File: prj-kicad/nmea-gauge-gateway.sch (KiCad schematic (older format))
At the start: 2 parts, among them P1 CONN_M12-5, P2 CONN_8

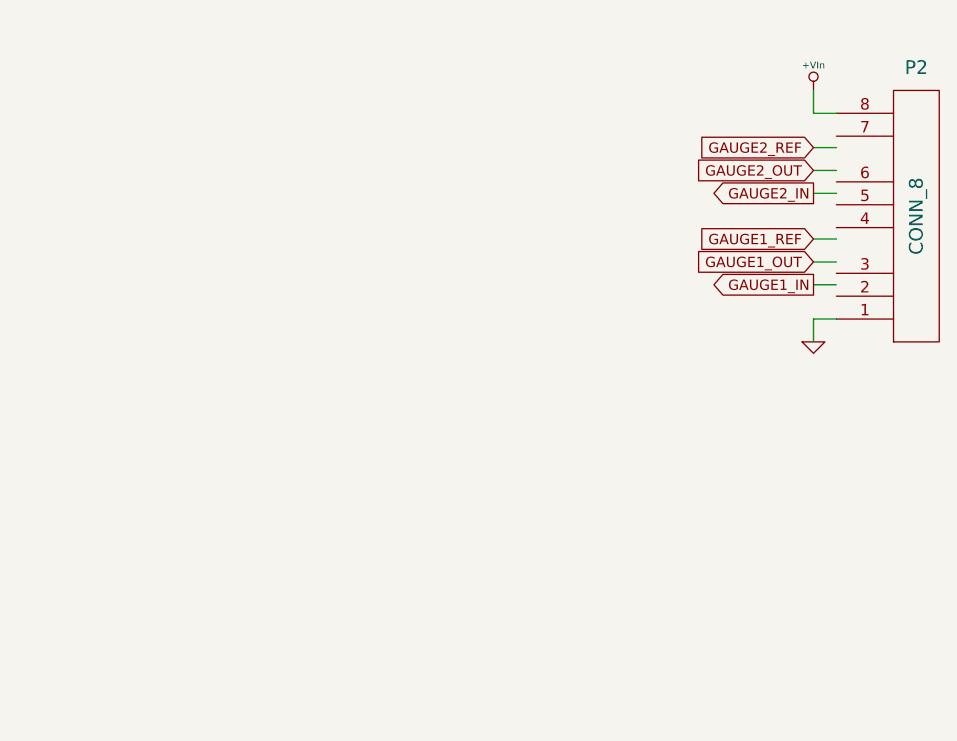
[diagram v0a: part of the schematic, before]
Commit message: = ADD: Insert analog inputs/outputs for gauge sensors
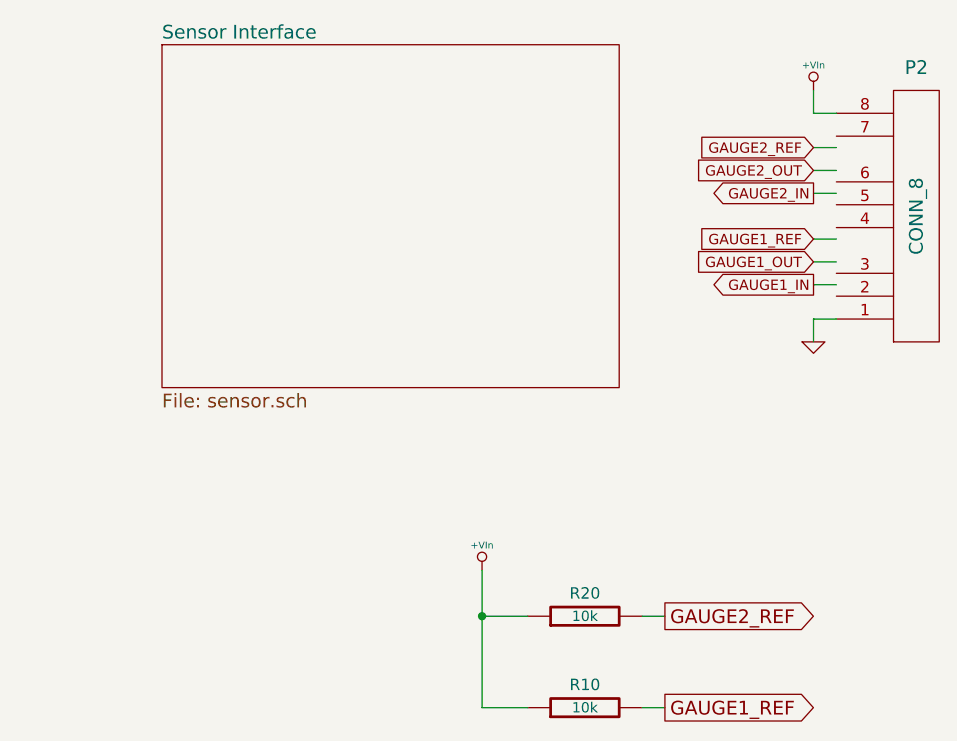
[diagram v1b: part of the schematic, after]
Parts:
- added R10, R20: 10k, nmea-gauge-gateway:SMD0805, symbol R
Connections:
- wire segments 10 -> 15
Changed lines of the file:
@@
 $Descr A4 11693 8268
 encoding utf-8
-Sheet 1 1
+Sheet 1 2
 Title "NMEA2000 Gauge Gateway"
 Date "2020-04-04"
@@
 F 0 "P1" H 1400 3700 60  0000 C CNN
 F 1 "CONN_M12-5" H 1400 3000 45  0000 C CNN
-F 2 "" H 1400 3350 60  0000 C CNN
+F 2 "" H 1400 3350 60  0001 C CNN
 F 3 "" H 1400 3350 60  0000 C CNN
 	1    1400 3350
 	-1   0    0    -1
 $EndComp
+$Comp
+L R R20
+U 1 1 5E9B72F1
+P 8600 5100
+F 0 "R20" V 8700 5100 50  0000 C CNN
+F 1 "10k" V 8600 5100 45  0000 C CNN
+F 2 "nmea-gauge-gateway:SMD0805" H 8600 5100 60  0001 C CNN
+F 3 "" H 8600 5100 60  0000 C CNN
+	1    8600 5100
+	0    -1   -1   0
+$EndComp
+$Comp
+L R R10
+U 1 1 5E9B7320
+P 8600 5500
+F 0 "R10" V 8700 5500 50  0000 C CNN
+F 1 "10k" V 8600 5500 45  0000 C CNN
+F 2 "nmea-gauge-gateway:SMD0805" H 8600 5500 60  0001 C CNN
+F 3 "" H 8600 5500 60  0000 C CNN
+	1    8600 5500
+	0    -1   -1   0
+$EndComp
+$Comp
+L +VIn #PWR03
+U 1 1 5E9B73E0
+P 8150 4900
+F 0 "#PWR03" H 8150 4860 30  0001 C CNN
+F 1 "+VIn" H 8150 5010 30  0000 C CNN
+F 2 "" H 8150 4900 60  0000 C CNN
+F 3 "" H 8150 4900 60  0000 C CNN
+	1    8150 4900
+	1    0    0    -1
+$EndComp
+Text GLabel 8950 5500 2    60   Output ~ 0
+GAUGE1_REF
+Wire Wire Line
+	8950 5500 8850 5500
+Wire Wire Line
+	8950 5100 8850 5100
+Text GLabel 8950 5100 2    60   Output ~ 0
+GAUGE2_REF
+Wire Wire Line
+	8150 4900 8150 5500
+Wire Wire Line
+	8150 5500 8350 5500
+Wire Wire Line
+	8350 5100 8150 5100
+Connection ~ 8150 5100
+$Sheet
+S 6750 2600 2000 1500
+U 5E920088
+F0 "Sensor Interface" 60
+F1 "sensor.sch" 60
+$EndSheet
 $EndSCHEMATC

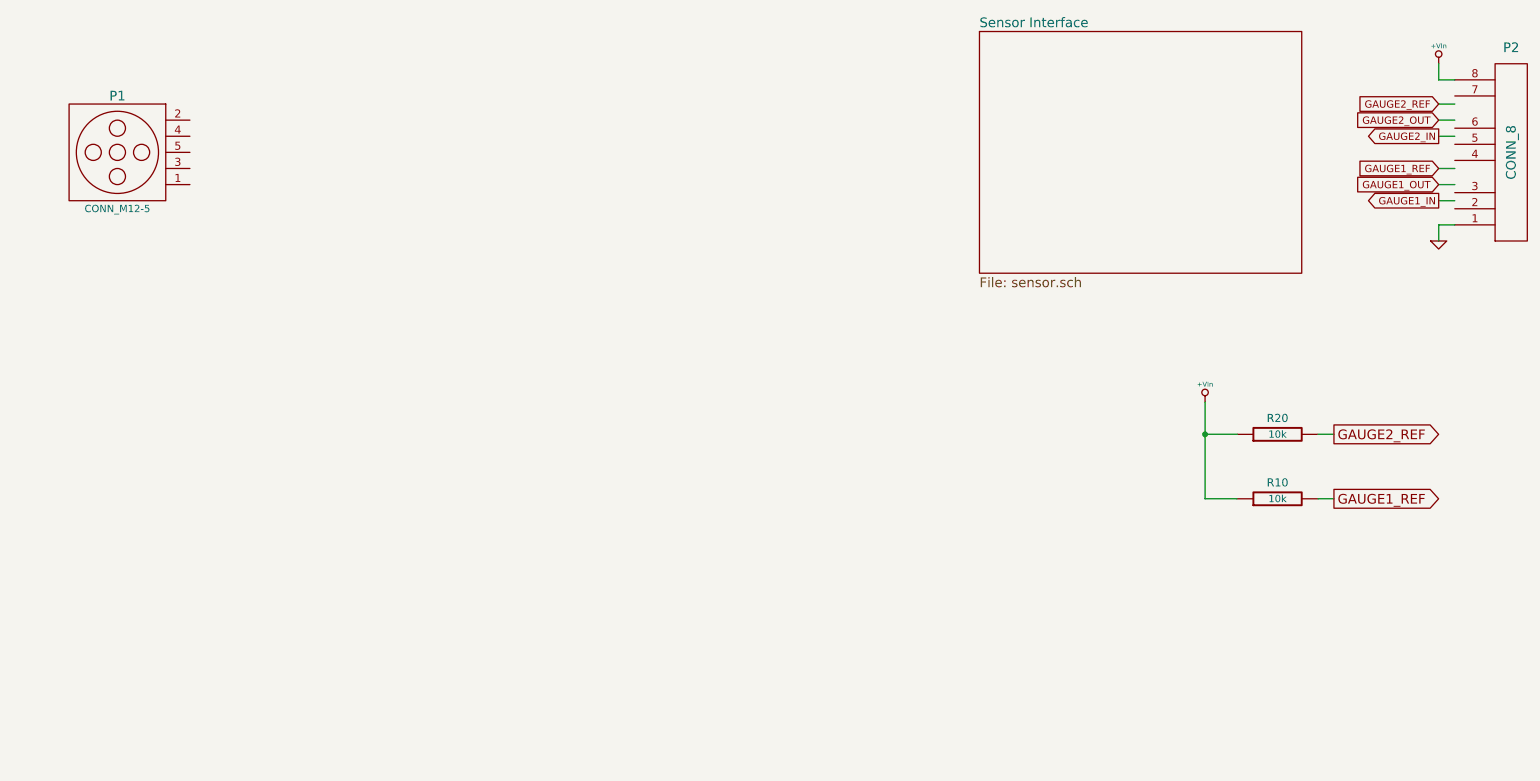
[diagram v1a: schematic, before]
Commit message: = ADD: Insert power supply
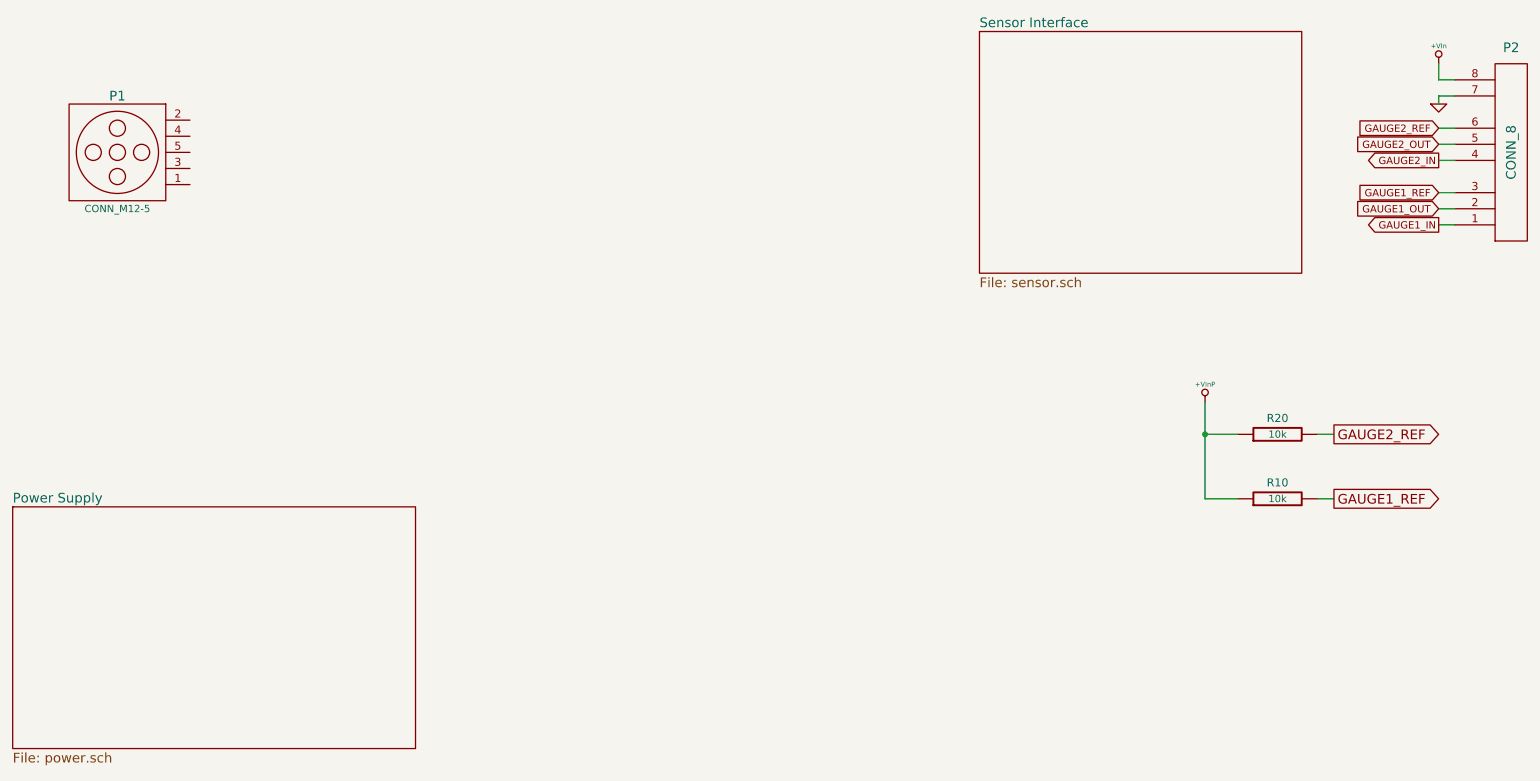
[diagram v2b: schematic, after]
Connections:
- net labels added: +VInP
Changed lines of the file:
@@
 $Descr A4 11693 8268
 encoding utf-8
-Sheet 1 2
+Sheet 1 3
 Title "NMEA2000 Gauge Gateway"
 Date "2020-04-04"
@@
 L GND #PWR01
 U 1 1 5E8895F5
-P 9600 3900
-F 0 "#PWR01" H 9600 3900 30  0001 C CNN
-F 1 "GND" H 9600 3830 30  0001 C CNN
-F 2 "" H 9600 3900 60  0000 C CNN
-F 3 "" H 9600 3900 60  0000 C CNN
-	1    9600 3900
+P 9600 3050
+F 0 "#PWR01" H 9600 3050 30  0001 C CNN
+F 1 "GND" H 9600 2980 30  0001 C CNN
+F 2 "" H 9600 3050 60  0000 C CNN
+F 3 "" H 9600 3050 60  0000 C CNN
+	1    9600 3050
 	1    0    0    -1
 $EndComp
 Wire Wire Line
-	9600 3900 9600 3800
+	9600 2900 9700 2900
+Text GLabel 9600 3800 0    45   Output ~ 0
+GAUGE1_IN
 Wire Wire Line
 	9600 3800 9700 3800
-Wire Wire Line
-	9600 2800 9600 2900
-Wire Wire Line
-	9600 2900 9700 2900
-$Comp
-L +VIn #PWR02
-U 1 1 5E889619
-P 9600 2800
-F 0 "#PWR02" H 9600 2760 30  0001 C CNN
-F 1 "+VIn" H 9600 2910 30  0000 C CNN
-F 2 "" H 9600 2800 60  0000 C CNN
-F 3 "" H 9600 2800 60  0000 C CNN
-	1    9600 2800
-	1    0    0    -1
-$EndComp
-Text GLabel 9600 3650 0    45   Output ~ 0
-GAUGE1_IN
-Wire Wire Line
-	9600 3650 9700 3650
-Text GLabel 9600 3550 0    45   Input ~ 0
+Text GLabel 9600 3700 0    45   Input ~ 0
 GAUGE1_OUT
-Text GLabel 9600 3450 0    45   Input ~ 0
+Text GLabel 9600 3600 0    45   Input ~ 0
 GAUGE1_REF
 Wire Wire Line
-	9600 3550 9700 3550
+	9600 3700 9700 3700
 Wire Wire Line
-	9700 3450 9600 3450
+	9700 3600 9600 3600
 Wire Wire Line
-	9600 3250 9700 3250
+	9600 3400 9700 3400
 Wire Wire Line
-	9600 3150 9700 3150
+	9600 3300 9700 3300
 Wire Wire Line
-	9600 3050 9700 3050
-Text GLabel 9600 3250 0    45   Output ~ 0
+	9600 3200 9700 3200
+Text GLabel 9600 3400 0    45   Output ~ 0
 GAUGE2_IN
-Text GLabel 9600 3150 0    45   Input ~ 0
+Text GLabel 9600 3300 0    45   Input ~ 0
 GAUGE2_OUT
-Text GLabel 9600 3050 0    45   Input ~ 0
+Text GLabel 9600 3200 0    45   Input ~ 0
 GAUGE2_REF
 $Comp
@@
 	0    -1   -1   0
 $EndComp
-$Comp
-L +VIn #PWR03
-U 1 1 5E9B73E0
-P 8150 4900
-F 0 "#PWR03" H 8150 4860 30  0001 C CNN
-F 1 "+VIn" H 8150 5010 30  0000 C CNN
-F 2 "" H 8150 4900 60  0000 C CNN
-F 3 "" H 8150 4900 60  0000 C CNN
-	1    8150 4900
-	1    0    0    -1
-$EndComp
 Text GLabel 8950 5500 2    60   Output ~ 0
 GAUGE1_REF
@@
 F1 "sensor.sch" 60
 $EndSheet
+$Sheet
+S 750  5550 2500 1500
+U 5E9581C6
+F0 "Power Supply" 60
+F1 "power.sch" 60
+$EndSheet
+Wire Wire Line
+	9600 3050 9600 3000
+Wire Wire Line
+	9600 3000 9700 3000
+Wire Wire Line
+	9600 2800 9600 2900
+$Comp
+L +VIn #PWR02
+U 1 1 5E889619
+P 9600 2800
+F 0 "#PWR02" H 9600 2760 30  0001 C CNN
+F 1 "+VIn" H 9600 2910 30  0000 C CNN
+F 2 "" H 9600 2800 60  0000 C CNN
+F 3 "" H 9600 2800 60  0000 C CNN
+	1    9600 2800
+	1    0    0    -1
+$EndComp
+$Comp
+L +VInP #PWR03
+U 1 1 5E95CB4C
+P 8150 4900
+F 0 "#PWR03" H 8150 4860 30  0001 C CNN
+F 1 "+VInP" H 8150 5010 30  0000 C CNN
+F 2 "" H 8150 4900 60  0000 C CNN
+F 3 "" H 8150 4900 60  0000 C CNN
+	1    8150 4900
+	1    0    0    -1
+$EndComp
 $EndSCHEMATC
